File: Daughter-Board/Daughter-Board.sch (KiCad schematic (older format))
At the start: 30 parts, among them P101 EdgeConn, P102 EdgeConn, U101 LMV934MA, U102 MC74VHCT126A, U103 MC74VHCT126A, U104 4016, U105 4016, U106 4016, U107 4016, U108 4016, U301 LM324A

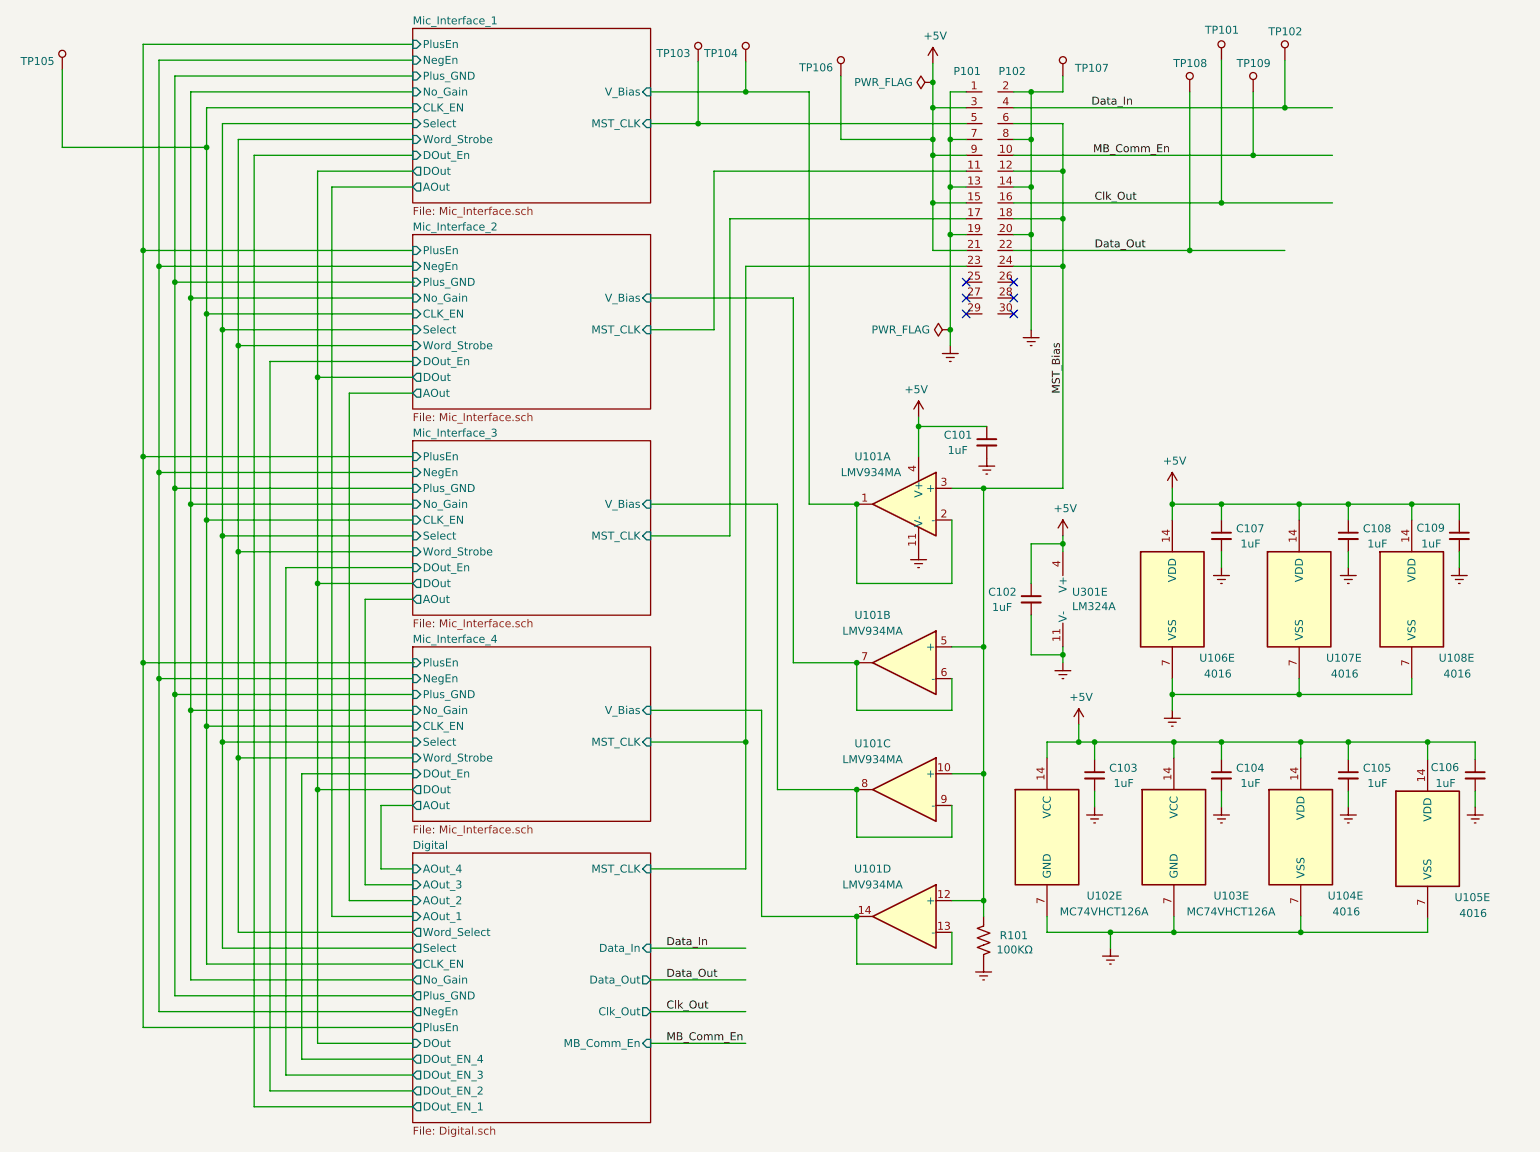
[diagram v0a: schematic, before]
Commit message: Add test points to Digital and Daughter-Board schematics
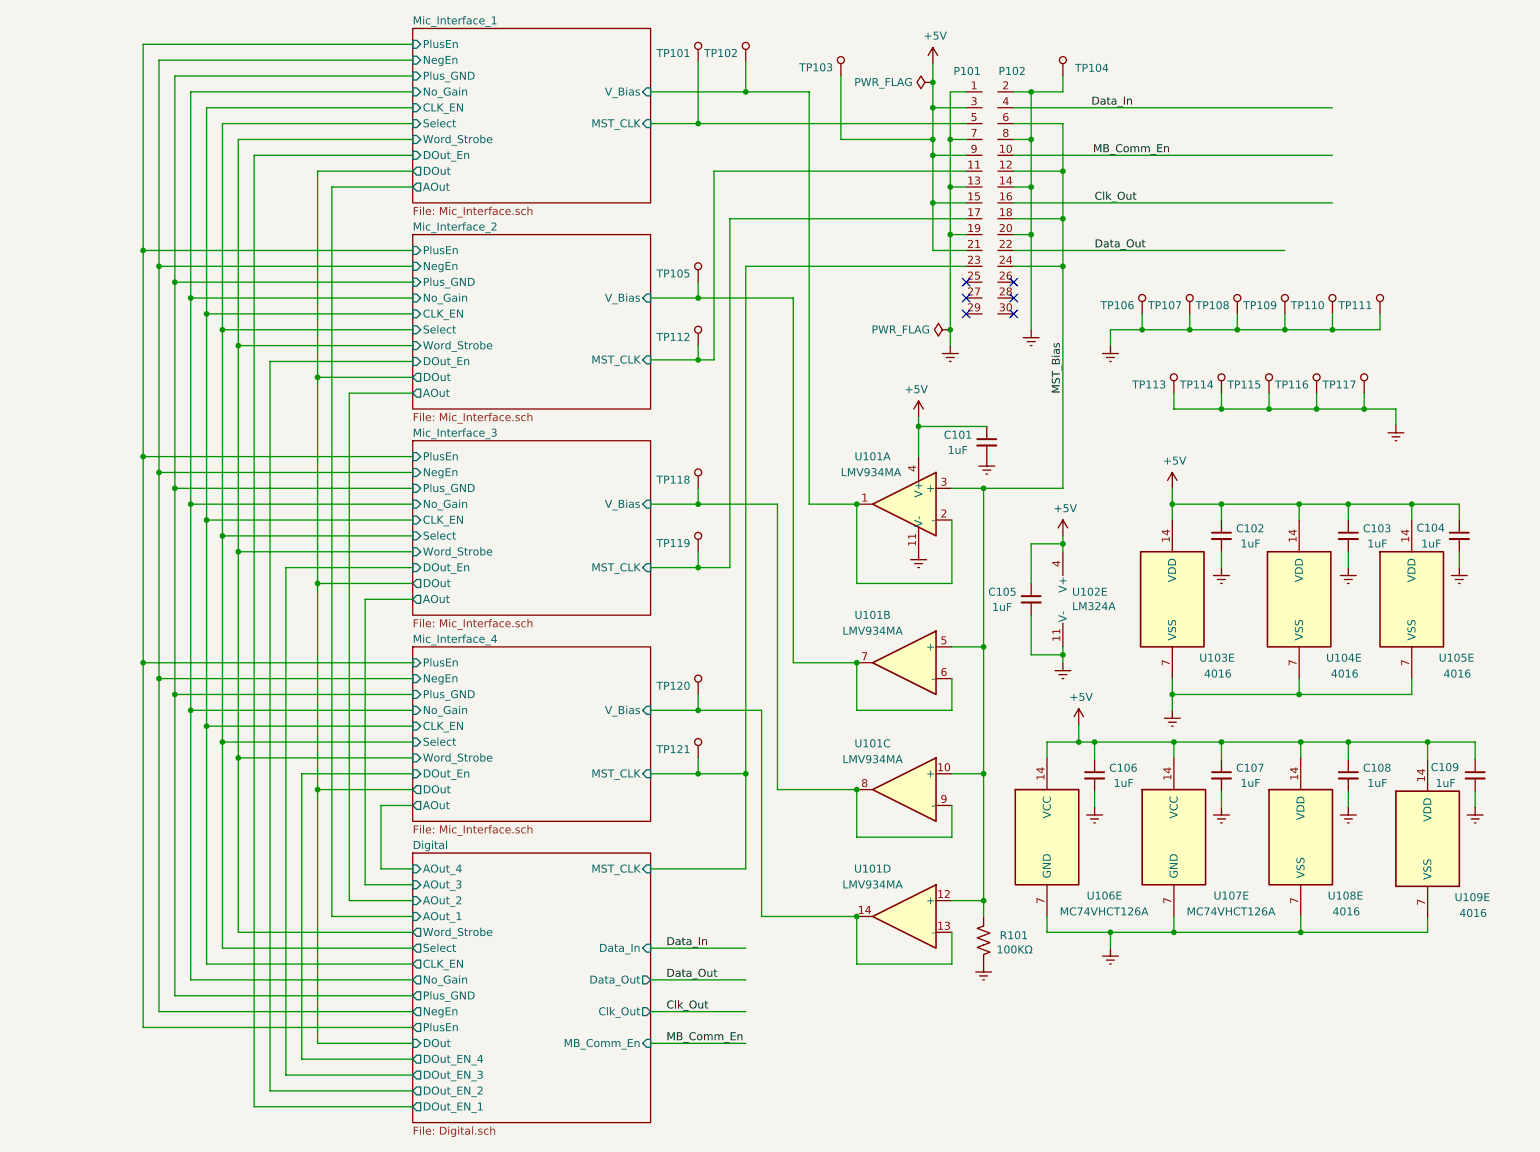
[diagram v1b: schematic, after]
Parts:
- removed TP101, TP102: 5000, digikey-footprints:Test_Point_D1.02mm, symbol dk_Test-Points:5000
- added TP106, TP107, TP110, TP111, TP112, TP113, TP114, TP115, TP116, TP117, TP118, TP119, TP120, TP121: 5000, digikey-footprints:Test_Point_D1.02mm, symbol dk_Test-Points:5000
- U102: renamed from U301; footprint Package_SO:TSSOP-14_4.4x5mm_P0.65mm -> Package_SO:SOIC-14_3.9x8.7mm_P1.27mm
- renumbered C107 to C102, C108 to C103, C109 to C104, C102 to C105, C103 to C106, C104 to C107, C105 to C108, C106 to C109, TP103 to TP101, TP104 to TP102, TP106 to TP103, TP107 to TP104, U106 to U103, U107 to U104, U108 to U105, U102 to U106, U103 to U107, U104 to U108, U105 to U109
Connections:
- wire segments 265 -> 290

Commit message: Add DigiKey # or Mouser # to component info, update footprintinfo for 14 and 20 pin devices.
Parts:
- U101: footprint Package_SO:TSSOP-14_4.4x5mm_P0.65mm -> Package_SO:SOIC-14_3.9x8.7mm_P1.27mm; Mouser # (none) -> 926-LMV934MA/NOPB
- U101: footprint Package_SO:TSSOP-14_4.4x5mm_P0.65mm -> Package_SO:SOIC-14_3.9x8.7mm_P1.27mm
- U103, U104, U105, U108, U109: value 4016 -> 74HC4016; DigiKey # (none) -> 296-CD74HC4016MTCT-ND
- U106, U107: Mouser # (none) -> 771-74VHCT126D118
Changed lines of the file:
@@
 F 0 "U101" H 7000 4000 50  0000 C CNN
 F 1 "LMV934MA" H 7010 3900 50  0000 C CNN
-F 2 "Package_SO:TSSOP-14_4.4x5mm_P0.65mm" H 6750 3800 50  0001 C CNN
-F 3 "" H 6850 3900 50  0001 C CNN
-F 4 "" H 6800 3700 50  0001 C CNN "DigiKey #"
+F 2 "Package_SO:SOIC-14_3.9x8.7mm_P1.27mm" H 6750 3800 50  0001 C CNN
+F 3 "~" H 6850 3900 50  0001 C CNN
+F 4 "926-LMV934MA/NOPB" H 6800 3700 50  0001 C CNN "Mouser #"
 	1    6800 3700
 	-1   0    0    -1
@@
 F 0 "U101" H 7000 5000 50  0000 C CNN
 F 1 "LMV934MA" H 7000 4900 50  0000 C CNN
-F 2 "Package_SO:TSSOP-14_4.4x5mm_P0.65mm" H 6750 4800 50  0001 C CNN
-F 3 "" H 6850 4900 50  0001 C CNN
+F 2 "Package_SO:SOIC-14_3.9x8.7mm_P1.27mm" H 6750 4800 50  0001 C CNN
+F 3 "~" H 6850 4900 50  0001 C CNN
+F 4 "926-LMV934MA/NOPB" H 6800 4700 50  0001 C CNN "Mouser #"
 	2    6800 4700
 	-1   0    0    -1
@@
 F 0 "U101" H 7000 5790 50  0000 C CNN
 F 1 "LMV934MA" H 7000 5690 50  0000 C CNN
-F 2 "Package_SO:TSSOP-14_4.4x5mm_P0.65mm" H 6750 5600 50  0001 C CNN
-F 3 "" H 6850 5700 50  0001 C CNN
+F 2 "Package_SO:SOIC-14_3.9x8.7mm_P1.27mm" H 6750 5600 50  0001 C CNN
+F 3 "~" H 6850 5700 50  0001 C CNN
 	3    6800 5500
 	-1   0    0    -1
@@
 F 0 "U101" H 7000 6600 50  0000 C CNN
 F 1 "LMV934MA" H 7000 6500 50  0000 C CNN
-F 2 "Package_SO:TSSOP-14_4.4x5mm_P0.65mm" H 6750 6400 50  0001 C CNN
-F 3 "" H 6850 6500 50  0001 C CNN
+F 2 "Package_SO:SOIC-14_3.9x8.7mm_P1.27mm" H 6750 6400 50  0001 C CNN
+F 3 "~" H 6850 6500 50  0001 C CNN
 	4    6800 6300
 	-1   0    0    -1
@@
 F 0 "U101" H 6748 3746 50  0001 L CNN
 F 1 "LMV934MA" H 6748 3655 50  0001 L CNN
-F 2 "Package_SO:TSSOP-14_4.4x5mm_P0.65mm" H 6740 3800 50  0001 C CNN
-F 3 "" H 6840 3900 50  0001 C CNN
+F 2 "Package_SO:SOIC-14_3.9x8.7mm_P1.27mm" H 6740 3800 50  0001 C CNN
+F 3 "~" H 6840 3900 50  0001 C CNN
+F 4 "926-LMV934MA/NOPB" H 6790 3700 50  0001 C CNN "Mouser #"
 	5    6790 3700
 	-1   0    0    -1
@@
 F 2 "Package_SO:SOIC-14_3.9x8.7mm_P1.27mm" H 8500 5800 50  0001 C CNN
 F 3 "http://www.ti.com/lit/gpn/sn74LS126" H 8500 5800 50  0001 C CNN
+F 4 "771-74VHCT126D118" H 8500 5800 50  0001 C CNN "Mouser #"
 	5    8500 5800
 	1    0    0    -1
@@
 F 2 "" H 7700 5800 50  0001 C CNN
 F 3 "http://www.ti.com/lit/gpn/sn74LS126" H 7700 5800 50  0001 C CNN
+F 4 "771-74VHCT126D118" H 7700 5800 50  0001 C CNN "Mouser #"
 	5    7700 5800
 	1    0    0    -1
@@
 P 9300 5800
 F 0 "U108" H 9470 5430 50  0000 L CNN
-F 1 "4016" H 9500 5330 50  0000 L CNN
+F 1 "74HC4016" H 9500 5330 50  0000 L CNN
 F 2 "Package_SO:SOIC-14_3.9x8.7mm_P1.27mm" H 9300 5800 50  0001 C CNN
 F 3 "http://www.ti.com/lit/ds/symlink/cd4016b.pdf" H 9300 5800 50  0001 C CNN
+F 4 "296-CD74HC4016MTCT-ND" H 9300 5800 50  0001 C CNN "DigiKey #"
 	5    9300 5800
 	1    0    0    -1
@@
 P 10100 5810
 F 0 "U109" H 10270 5440 50  0000 L CNN
-F 1 "4016" H 10300 5340 50  0000 L CNN
+F 1 "74HC4016" H 10300 5340 50  0000 L CNN
 F 2 "Package_SO:SOIC-14_3.9x8.7mm_P1.27mm" H 10100 5810 50  0001 C CNN
 F 3 "http://www.ti.com/lit/ds/symlink/cd4016b.pdf" H 10100 5810 50  0001 C CNN
+F 4 "296-CD74HC4016MTCT-ND" H 10100 5810 50  0001 C CNN "DigiKey #"
 	5    10100 5810
 	1    0    0    -1
@@
 P 8490 4300
 F 0 "U103" H 8660 3930 50  0000 L CNN
-F 1 "4016" H 8690 3830 50  0000 L CNN
+F 1 "74HC4016" H 8690 3830 50  0000 L CNN
 F 2 "Package_SO:SOIC-14_3.9x8.7mm_P1.27mm" H 8490 4300 50  0001 C CNN
 F 3 "http://www.ti.com/lit/ds/symlink/cd4016b.pdf" H 8490 4300 50  0001 C CNN
+F 4 "296-CD74HC4016MTCT-ND" H 8490 4300 50  0001 C CNN "DigiKey #"
 	5    8490 4300
 	1    0    0    -1
@@
 P 9290 4300
 F 0 "U104" H 9460 3930 50  0000 L CNN
-F 1 "4016" H 9490 3830 50  0000 L CNN
+F 1 "74HC4016" H 9490 3830 50  0000 L CNN
 F 2 "Package_SO:SOIC-14_3.9x8.7mm_P1.27mm" H 9290 4300 50  0001 C CNN
 F 3 "http://www.ti.com/lit/ds/symlink/cd4016b.pdf" H 9290 4300 50  0001 C CNN
+F 4 "296-CD74HC4016MTCT-ND" H 9290 4300 50  0001 C CNN "DigiKey #"
 	5    9290 4300
 	1    0    0    -1
@@
 P 10000 4300
 F 0 "U105" H 10170 3930 50  0000 L CNN
-F 1 "4016" H 10200 3830 50  0000 L CNN
+F 1 "74HC4016" H 10200 3830 50  0000 L CNN
 F 2 "Package_SO:SOIC-14_3.9x8.7mm_P1.27mm" H 10000 4300 50  0001 C CNN
 F 3 "http://www.ti.com/lit/ds/symlink/cd4016b.pdf" H 10000 4300 50  0001 C CNN
+F 4 "296-CD74HC4016MTCT-ND" H 10000 4300 50  0001 C CNN "DigiKey #"
 	5    10000 4300
 	1    0    0    -1

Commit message: Corrected analog gain switch position.
Analog gain switch was across the feedback resistor. It is changed to grounding of the - input resistor to the op amp.
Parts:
- renumbered C105 to C102, C102 to C103, C103 to C104, C104 to C105
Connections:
- wire segments 290 -> 289
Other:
- moved on the sheet: C102, TP113, TP114, TP115, TP116, TP117, U102E

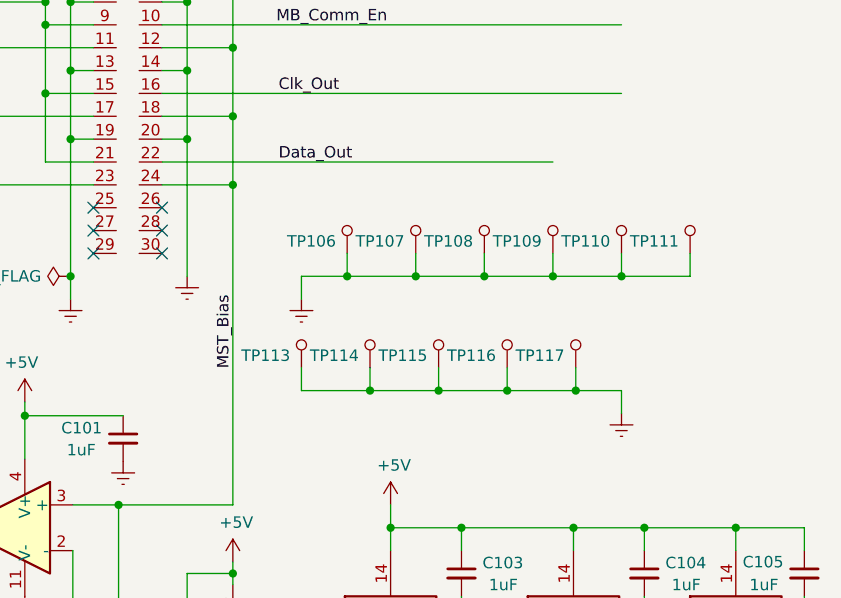
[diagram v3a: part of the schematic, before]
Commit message: Add connector for PICkit to MCU interface.
In the process of adding the PICkit connector some control lines had to be moved.
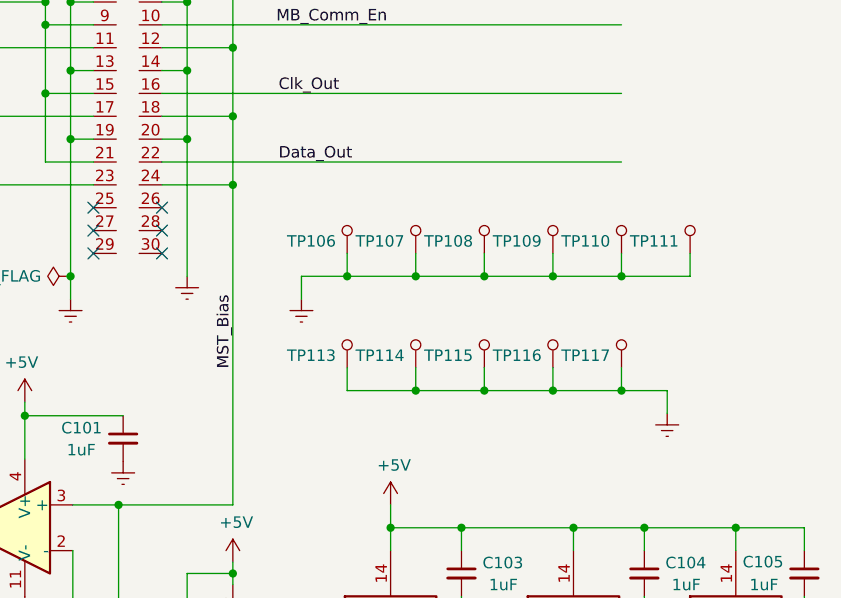
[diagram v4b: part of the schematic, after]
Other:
- moved on the sheet: TP113, TP114, TP115, TP116, TP117

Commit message: Modify schematic to recover PCB layout.
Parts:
- removed TP108, TP109, TP110, TP111, TP113, TP114, TP115, TP116, TP117: 5000, digikey-footprints:Test_Point_D1.02mm, symbol dk_Test-Points:5000
- C101, C102, C103, C104, C105, C106, C107, C108, C109: footprint Capacitor_SMD:C_1206_3216Metric -> Capacitor_SMD:C_0805_2012Metric
- R101: footprint Resistor_SMD:R_1206_3216Metric -> Resistor_SMD:R_0805_2012Metric
- TP101, TP102, TP103, TP104, TP105, TP106, TP107, TP112, TP118, TP119, TP120, TP121: footprint digikey-footprints:Test_Point_D1.02mm -> TestPoint:TestPoint_Pad_D1.0mm
- U101, U102, U107: footprint Package_SO:SOIC-14_3.9x8.7mm_P1.27mm -> Package_SO:TSSOP-14_4.4x5mm_P0.65mm
- U106: footprint (none) -> Package_SO:SOIC-14_3.9x8.7mm_P1.27mm
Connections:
- net labels added: AOut_1, AOut_2, AOut_3, AOut_4, MIC_MST_CLK_1, MIC_MST_CLK_2, MIC_MST_CLK_3, MIC_MST_CLK_4, V_BIAS_1, V_BIAS_2, V_BIAS_3, V_BIAS_4
- wire segments 289 -> 270
